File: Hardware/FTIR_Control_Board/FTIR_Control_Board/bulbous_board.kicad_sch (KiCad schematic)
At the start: 20 parts, among them J1 RJ45_LED_Shielded, Q1 NMOS, U1 Peensy4.1_DEV-16771, U2 OKI, U4 TMC2208

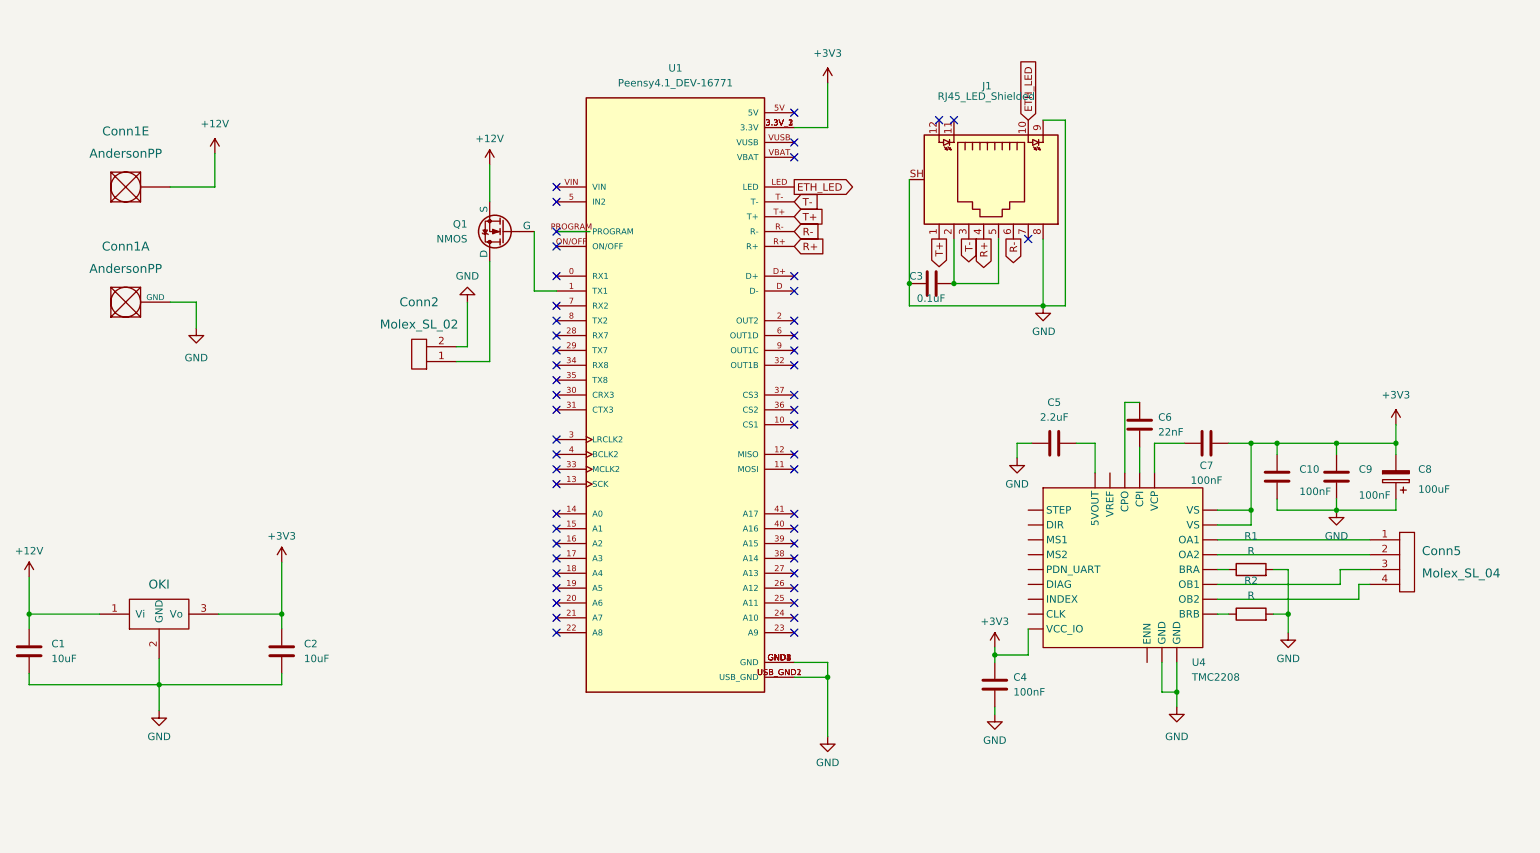
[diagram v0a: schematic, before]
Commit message: Stepper Driver work and general clean-up
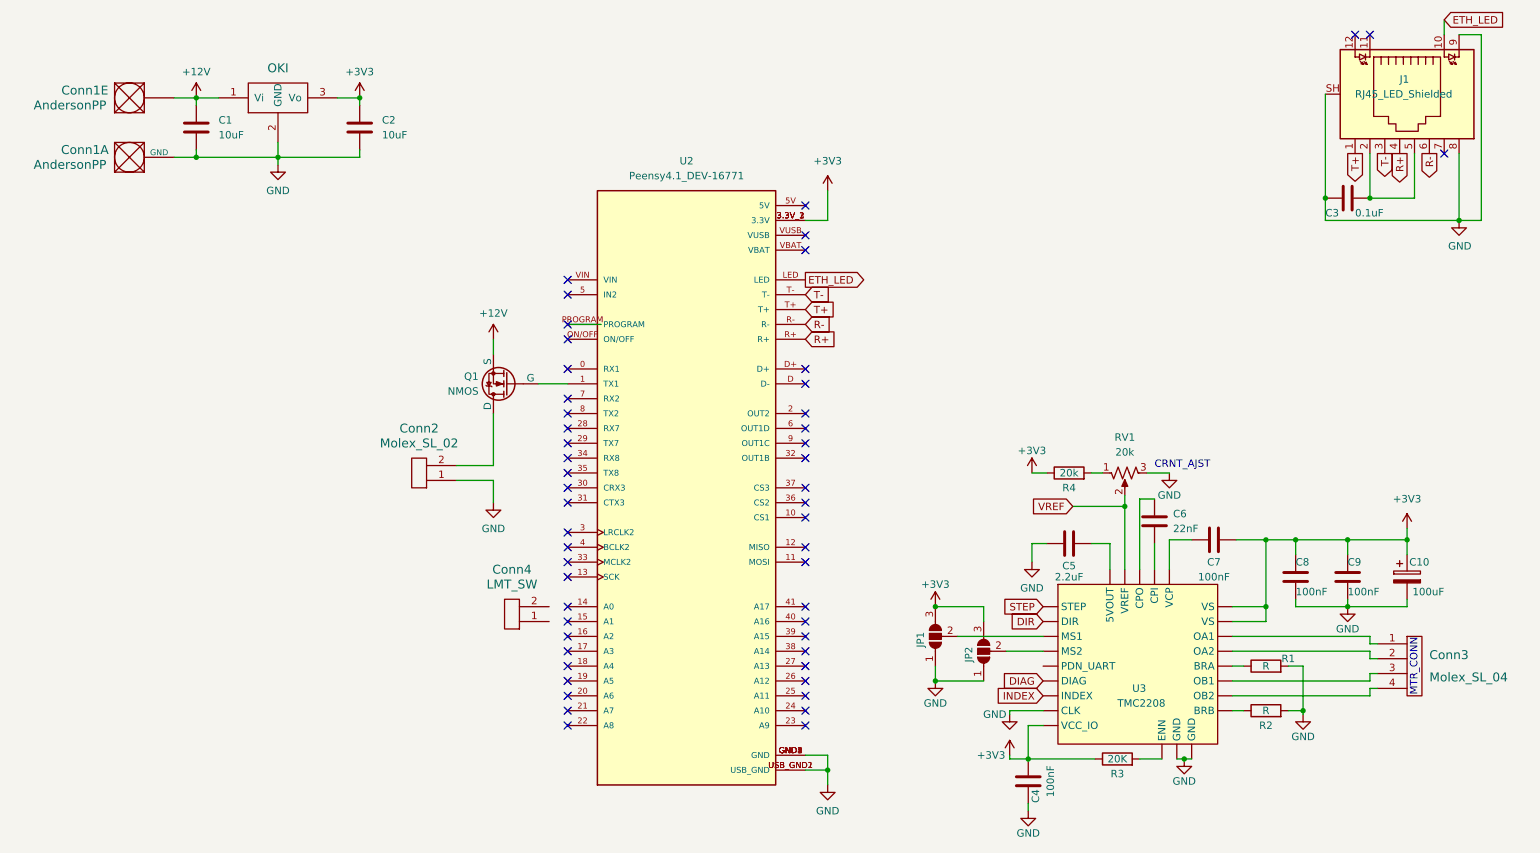
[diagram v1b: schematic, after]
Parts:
- added Conn4: LMT_SW, symbol MRDT_Connectors:Molex_SL_02
- added JP1, JP2: SolderJumper_3_Open, symbol Jumper:SolderJumper_3_Open
- added R3: 20K, symbol Device:R
- added R4: 20k, symbol Device:R
- added RV1: 20k, symbol Device:R_Potentiometer_US
- renumbered C8 to C10, C10 to C8, Conn5 to Conn3, U2 to U1, U1 to U2, U4 to U3
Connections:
- net +3V3: now also C10.1, C4.1, JP1.3 (B), JP2.3 (B), R3.1, R4.1; no longer C10.2, C4.2
- net GND: now also C10.2, C4.2, Conn2.1, JP1.1 (A), JP2.1 (A), RV1.3; no longer C10.1, C4.1, Conn2.2
- net VREF: now reaches U3. (VS)
- net VREF: now also RV1.2
- net at Q1.1 (D): now also Conn2.2; no longer Conn2.1
- new net: JP2.2 (C), U3. (VS)
- new net: R4.2, RV1.1
- new net: R3.2, U3. (VS)
- new net: JP1.2 (C), U3. (VS)
- new net DIAG: U3. (VS)
- new net DIR: U3. (VS)
- new net INDEX: U3. (VS)
- new net STEP: U3. (VS)
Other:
- note added: "CRNT_AJST"
- note added: "MTR_CONN"
- moved on the sheet: C1, C10, C2, C3, C4, C5, C6, C7, C8, C9, Conn1A, Conn1E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
